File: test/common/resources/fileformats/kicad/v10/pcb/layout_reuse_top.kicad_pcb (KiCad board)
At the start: 2 copper layers, 9 parts

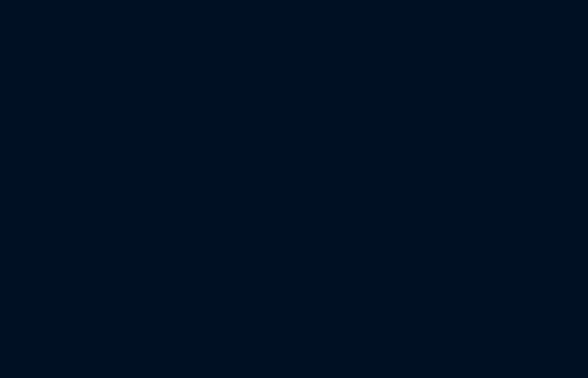
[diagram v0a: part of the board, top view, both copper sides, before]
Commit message: Feat: v10 net model — name-only references, synthesized numbering (P0.2 S4)
Breaking point ① of the v9->v10 dialect migration (BACKLOG M0+M1).
The Python-visible model is unchanged (segment.net stays int, pad.net stays
Net{number,name}) — numbers become process-internal handles entirely inside
the zig layer, so all 21 Python consumer sites keep working until S6.

Read (v10): PcbFile.loads sniffs (version >= 20250000), pre-scans every
'(net "name")' reference from the token tree, synthesizes the numbering by
the pinned M0 rule (byte-wise sorted unique names -> 1..n, "" always 0 —
reference-order independent and process-deterministic by construction),
resolves name->number during decode via the new net_ref SexpField flag, and
materializes pcb.nets (v10 files have no table). v9 path: zero changes.

Write (v10): net_ref fields emit the resolved name, never a number; net 0
omits the clause entirely (keepout zones); the net table, zone net_name and
the pad-net name slot are suppressed via v9_only. v9 writes byte-identical.

Also: Property.at/layer now optional — KiCad 10 writes bare metadata
properties like '(property ki_fp_filters "C_*")' (blocked lvds parse);
v9 layout_reuse fixture regained its manual segment (its named group had a
dangling member, which kicad-cli upgrade silently cleaned away) and the v10
pair + snapshots were regenerated; Python version guard ceiling -> 20260206.

转绿 (21 个开关): corpus parse x4 + 幂等 x4 + 语义快照 x4 (v10 REGEN; test
板 v9/v10 快照逐字节相同) + 跨方言等价 x3 + T4 v10 契约 x4 (引用序无关、
跨进程确定性) + S0 合成规则契约 + S0 KiCad 重存语义回环 oracle (提前转绿,
XPASS 棘轮捕获后摘标)。
保持绿: libs/kicad+exporters 133 passed + 8 xfailed (恰为 S5 的 7 个 +
S7 的 DRC oracle); E2E determinism 4/4 (225s)。
T8 变异自检: 植入按出现序编号 (去排序+线性查找) -> 唯一红灯 = S0 合成规则
契约 (语义视图按名解析, 对一致重编号天然失明); 恢复后全绿。

Co-Authored-By: Claude Fable 5 <noreply@anthropic.com>
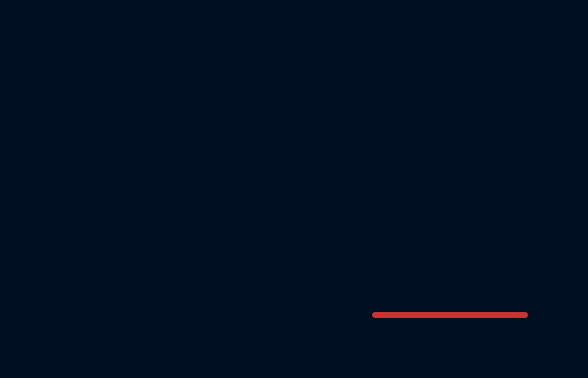
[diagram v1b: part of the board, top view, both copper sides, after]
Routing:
- net unnamed[0]: track 0.00 -> 5.00 mm
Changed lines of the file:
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@@
+	)
+	(segment
+		(start 95 95)
+		(end 100 95)
+		(width 0.2)
+		(layer "F.Cu")
+		(net "unnamed[0]")
 	)
 	(segment
@@
 		)
 	)
+	(group "manual_human_group"
+		(members "11111111-2222-3333-4444-555555555555")
+	)
 	(group "sub_chains[0]"
